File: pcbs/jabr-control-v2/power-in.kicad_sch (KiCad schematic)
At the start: 9 parts, among them J9001 43045-0201, U301 TVS3301DRBR, U302 TPS26600RHFR

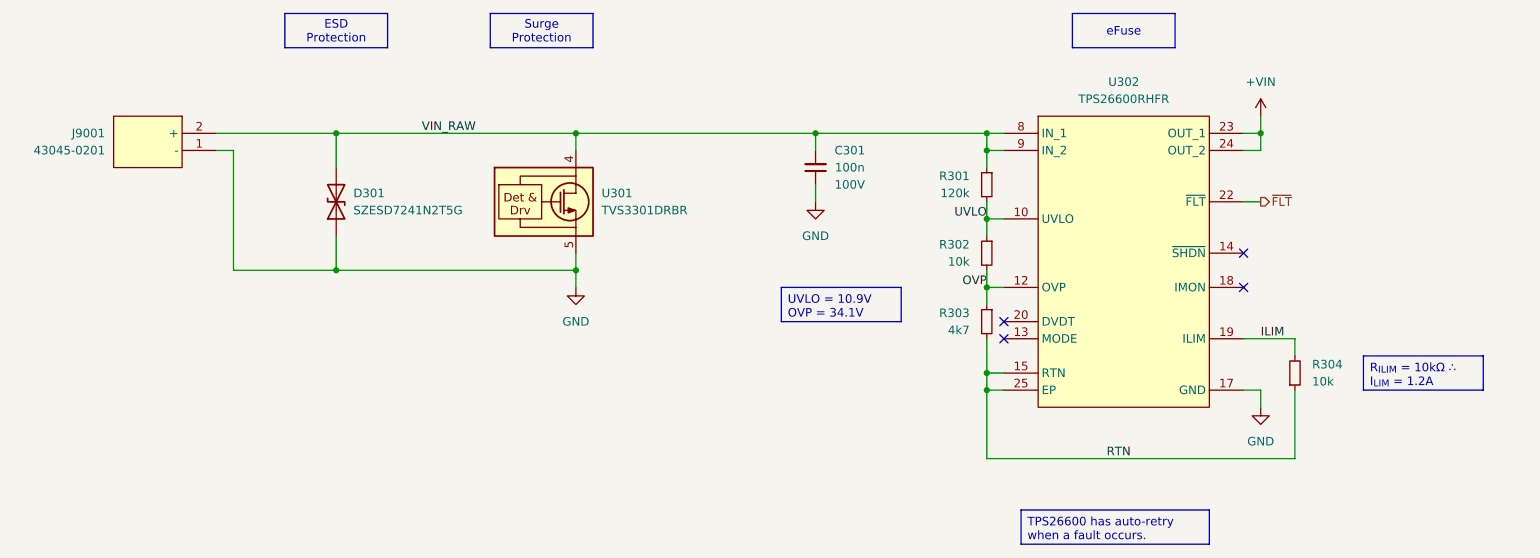
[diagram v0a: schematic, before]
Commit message: PCI11010C Schematic sheet mostly done
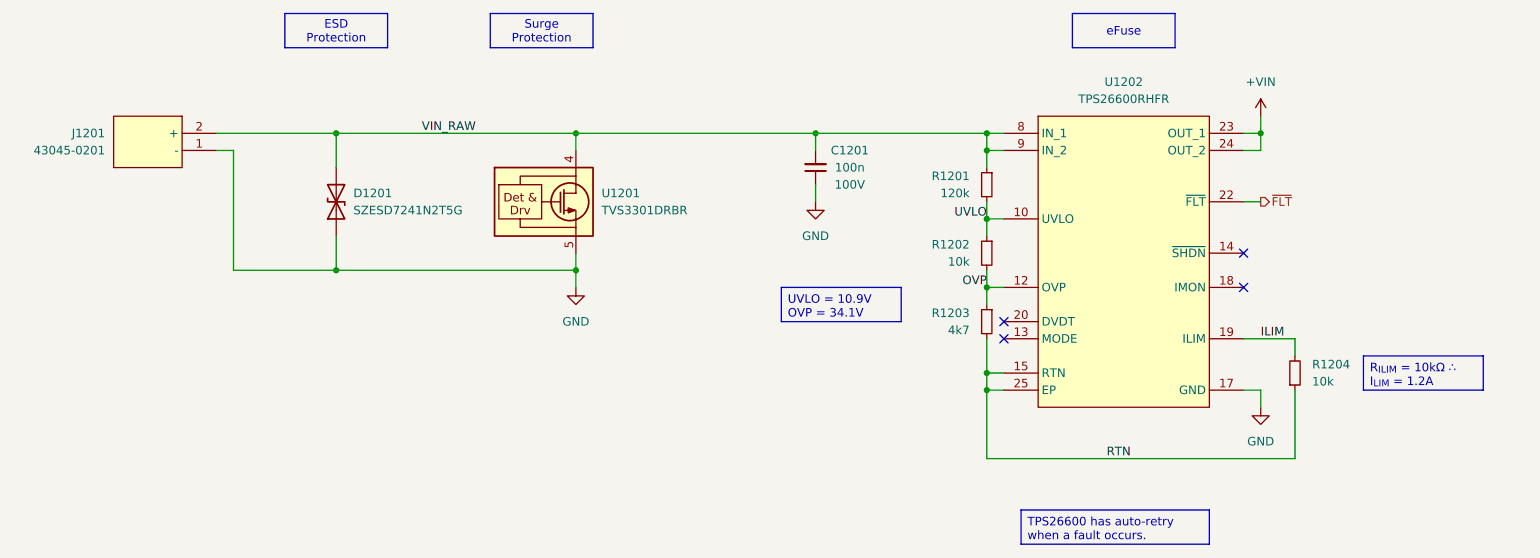
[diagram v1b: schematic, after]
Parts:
- renumbered C301 to C1201, D301 to D1201, J9001 to J1201, R301 to R1201, R302 to R1202, R303 to R1203, R304 to R1204, U301 to U1201, U302 to U1202

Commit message: Power circuitry done
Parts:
- added R1205: 22k, project_footprints:R_0402, symbol Device:R_Small
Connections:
- net ILIM: now also R1205.2
- net RTN: now also R1205.1
- net ~{FLT}: no longer names the net of U1202.22 (~{FLT})
- no-connect marks 4 -> 5
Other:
- moved on the sheet: R1204
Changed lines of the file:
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@@
 		)
 	)
-	(text_box "R_{ILIM} = 10kΩ ∴ I_{LIM} = 1.2A"
+	(text_box "R_{ILIM} = 6.9kΩ ∴ I_{LIM} = 1.75A"
 		(exclude_from_sim no)
-		(at 238.76 109.22 0)
-		(size 17.78 5.08)
+		(at 231.14 98.1471 0)
+		(size 17.78 5.9929)
 		(margins 0.9525 0.9525 0.9525 0.9525)
 		(stroke
@@
 				(size 1.27 1.27)
 			)
-			(justify left top)
+			(justify left)
 		)
 	)
@@
 	)
 	(junction
+		(at 231.14 106.68)
+		(diameter 0)
+		(color 0 0 0 0)
+	)
+	(junction
 		(at 182.88 78.74)
 		(diameter 0)
@@
 		(color 0 0 0 0)
 	)
+	(junction
+		(at 231.14 124.46)
+		(diameter 0)
+		(color 0 0 0 0)
+	)
 	(no_connect
 		(at 185.42 104.14)
@@
 	)
 	(no_connect
+		(at 220.98 86.36)
+	)
+	(no_connect
 		(at 220.98 93.98)
 	)
@@
 	(wire
 		(pts
-			(xy 228.6 124.46) (xy 182.88 124.46)
+			(xy 243.84 109.22) (xy 243.84 106.68)
 		)
 		(stroke
@@
 	(wire
 		(pts
-			(xy 228.6 114.3) (xy 228.6 124.46)
+			(xy 231.14 114.3) (xy 231.14 124.46)
 		)
 		(stroke
@@
 	(wire
 		(pts
-			(xy 220.98 106.68) (xy 228.6 106.68)
+			(xy 220.98 106.68) (xy 231.14 106.68)
 		)
 		(stroke
@@
 	(wire
 		(pts
-			(xy 228.6 109.22) (xy 228.6 106.68)
+			(xy 231.14 109.22) (xy 231.14 106.68)
 		)
 		(stroke
@@
 	(wire
 		(pts
-			(xy 220.98 86.36) (xy 223.52 86.36)
-		)
-		(stroke
-			(width 0)
-			(type default)
-		)
-	)
-	(wire
-		(pts
 			(xy 68.58 78.74) (xy 71.12 78.74)
 		)
@@
 	(wire
 		(pts
+			(xy 243.84 114.3) (xy 243.84 124.46)
+		)
+		(stroke
+			(width 0)
+			(type default)
+		)
+	)
+	(wire
+		(pts
 			(xy 157.48 76.2) (xy 182.88 76.2)
 		)
@@
 	(wire
 		(pts
+			(xy 182.88 124.46) (xy 231.14 124.46)
+		)
+		(stroke
+			(width 0)
+			(type default)
+		)
+	)
+	(wire
+		(pts
+			(xy 231.14 106.68) (xy 243.84 106.68)
+		)
+		(stroke
+			(width 0)
+			(type default)
+		)
+	)
+	(wire
+		(pts
 			(xy 182.88 86.36) (xy 182.88 88.9)
 		)
@@
 		(pts
 			(xy 185.42 78.74) (xy 182.88 78.74)
+		)
+		(stroke
+			(width 0)
+			(type default)
+		)
+	)
+	(wire
+		(pts
+			(xy 243.84 124.46) (xy 231.14 124.46)
 		)
 		(stroke
@@
 			)
 			(justify left bottom)
-		)
-	)
-	(hierarchical_label "~{FLT}"
-		(shape output)
-		(at 223.52 86.36 0)
-		(effects
-			(font
-				(size 1.27 1.27)
-			)
-			(justify left)
 		)
 	)
@@
 	(symbol
 		(lib_id "Device:R_Small")
-		(at 228.6 111.76 0)
+		(at 231.14 111.76 0)
 		(mirror x)
 		(unit 1)
@@
 		(dnp no)
 		(property "Reference" "R1204"
-			(at 231.14 110.4901 0)
+			(at 233.68 110.4901 0)
 			(show_name no)
 			(do_not_autoplace no)
@@
 		)
 		(property "Value" "10k"
-			(at 231.14 113.0301 0)
+			(at 233.68 113.0301 0)
 			(show_name no)
 			(do_not_autoplace no)
@@
 		)
 		(property "Footprint" "project_footprints:R_0402"
-			(at 228.6 111.76 0)
+			(at 231.14 111.76 0)
 			(hide yes)
 			(show_name no)
@@
 		)
 		(property "Datasheet" ""
-			(at 228.6 111.76 0)
+			(at 231.14 111.76 0)
 			(hide yes)
 			(show_name no)
@@
 		)
 		(property "Description" "Resistor, small symbol"
-			(at 228.6 111.76 0)
+			(at 231.14 111.76 0)
 			(hide yes)
 			(show_name no)
@@
 		)
 		(property "Field6" ""
-			(at 228.6 111.76 0)
+			(at 231.14 111.76 0)
 			(hide yes)
 			(show_name no)
@@
 		)
 		(property "Field7" ""
-			(at 228.6 111.76 0)
+			(at 231.14 111.76 0)
 			(hide yes)
 			(show_name no)
@@
 		)
 		(property "Part Description" ""
-			(at 228.6 111.76 0)
+			(at 231.14 111.76 0)
 			(hide yes)
 			(show_name no)
@@
 					(unit 1)
 				)
+			)
+		)
+	)
+	(symbol
+		(lib_id "Device:R_Small")
+		(at 243.84 111.76 0)
+		(mirror x)
+		(unit 1)
+		(body_style 1)
+		(exclude_from_sim no)
+		(in_bom yes)
+		(on_board yes)
+		(in_pos_files yes)
+		(dnp no)
+		(property "Reference" "R1205"
+			(at 246.38 110.4901 0)
+			(show_name no)
+			(do_not_autoplace no)
+			(effects
+				(font
+					(size 1.27 1.27)
+				)
+				(justify left)
+			)
+		)
+		(property "Value" "22k"
+			(at 246.38 113.0301 0)
+			(show_name no)
+			(do_not_autoplace no)
+			(effects
+				(font
+					(size 1.27 1.27)
+				)
+				(justify left)
+			)
+		)
+		(property "Footprint" "project_footprints:R_0402"
+			(at 243.84 111.76 0)
+			(hide yes)
+			(show_name no)
+			(do_not_autoplace no)
+			(effects
+				(font
+					(size 1.27 1.27)
+				)
+			)
+		)
+		(property "Datasheet" ""
+			(at 243.84 111.76 0)
+			(hide yes)
+			(show_name no)
+			(do_not_autoplace no)
+			(effects
+				(font
+					(size 1.27 1.27)
+				)
+			)
+		)
+		(property "Description" "Resistor, small symbol"
+			(at 243.84 111.76 0)
+			(hide yes)
+			(show_name no)
+			(do_not_autoplace no)
+			(effects
+				(font
+					(size 1.27 1.27)
+				)
+			)
+		)
+		(property "Field6" ""
+			(at 243.84 111.76 0)
+			(hide yes)
+			(show_name no)
+			(do_not_autoplace no)
+			(effects
+				(font
+					(size 1.27 1.27)
+				)
+			)
+		)
+		(property "Field7" ""
+			(at 243.84 111.76 0)
+			(hide yes)
+			(show_name no)
+			(do_not_autoplace no)
+			(effects
+				(font
+					(size 1.27 1.27)
+				)
+			)
+		)
+		(property "Part Description" ""
+			(at 243.84 111.76 0)
+			(hide yes)
+			(show_name no)
+			(do_not_autoplace no)
+			(effects
+				(font
+					(size 1.27 1.27)
+				)
+			)
+		)
+		(pin "1"
+		)
+		(pin "2"
+		)
+		(instances
+			(project "jabr-control-v2"
+				(path "/f91ec272-d09a-4038-bbbb-962739a92c51/3f551047-3bb0-4f63-99e0-34fd9061d844/c8847476-18c7-4518-a86a-3cbd7effb778"
+					(reference "R1205")
+					(unit 1)
+				)

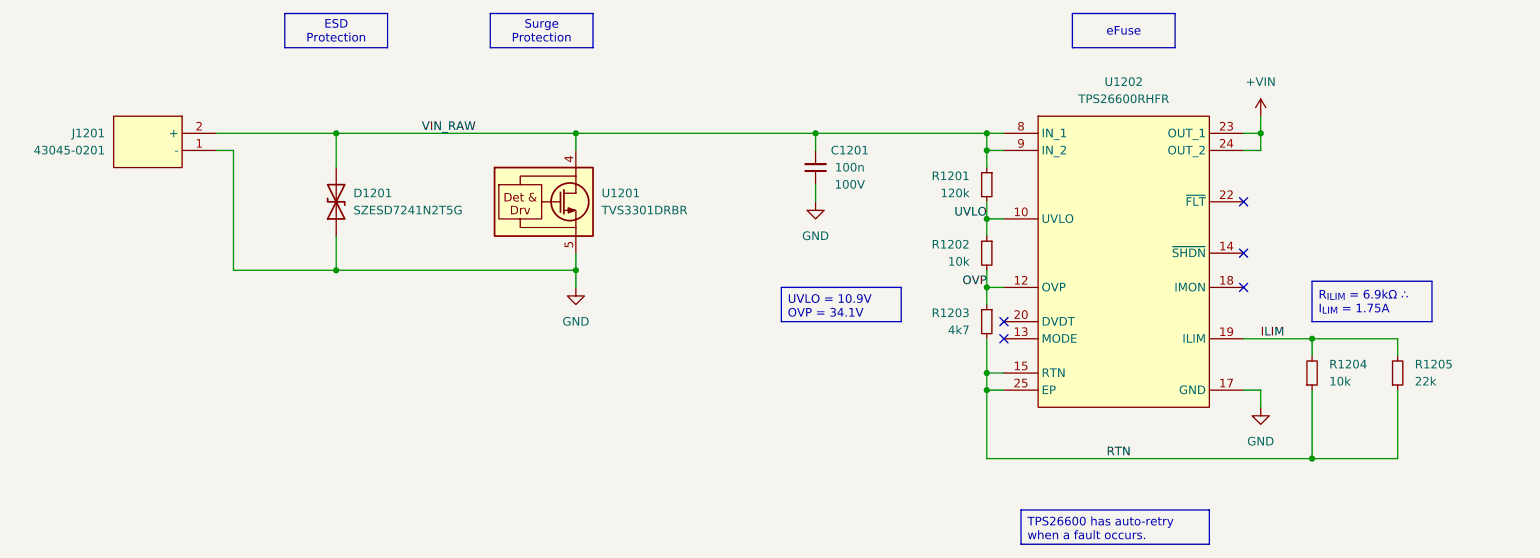
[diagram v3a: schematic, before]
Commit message: Schematic done
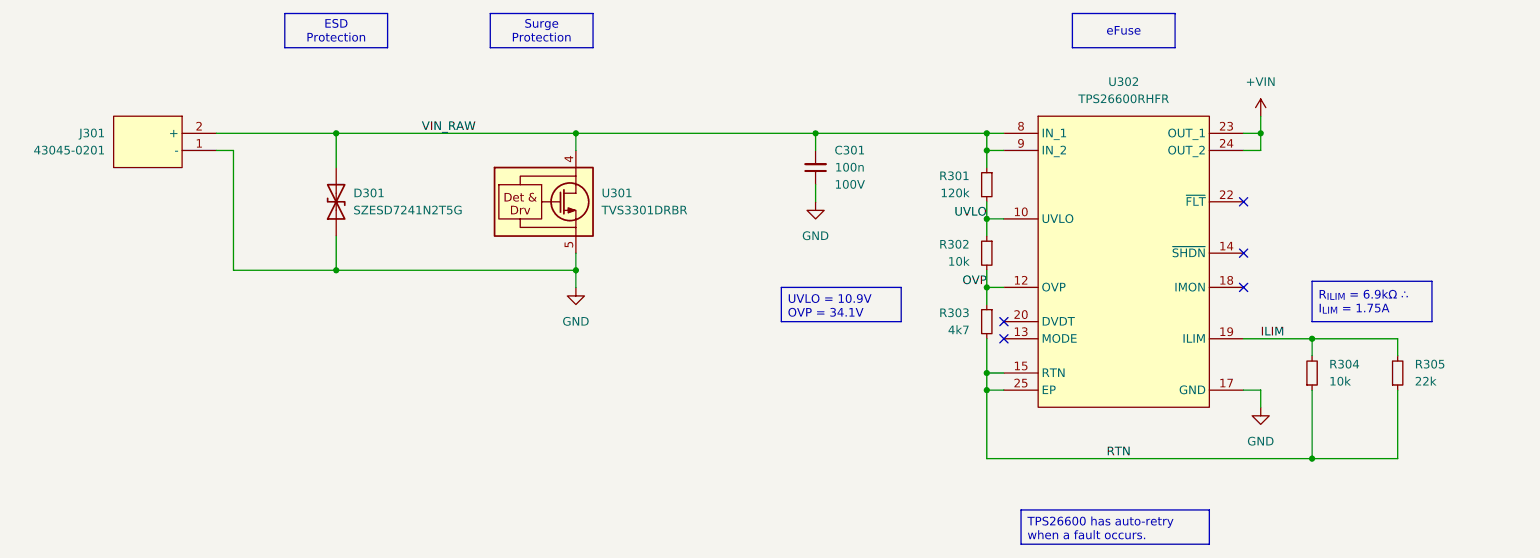
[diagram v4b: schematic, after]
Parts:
- renumbered C1201 to C301, D1201 to D301, J1201 to J301, R1201 to R301, R1202 to R302, R1203 to R303, R1204 to R304, R1205 to R305, U1201 to U301, U1202 to U302
